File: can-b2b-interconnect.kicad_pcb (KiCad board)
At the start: 2 copper layers, 6.3 x 13.1 mm, 4 parts, among them U1 DF52-4S-0.8H(21), U2 DF52-4S-0.8H(21), U3 DF52-4S-0.8H(21)

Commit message: not routed yet, sch
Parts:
- removed U2, U3: DF52-4S-0.8H(21), can-b2b-interconnect:DF52-4S-0.8H(21)
- added J1: USB4110GFA, can-b2b-interconnect:GCT_USB4105-GF-A, F.Cu at (102.5, 63.5)
- added J2: USB4110GFA, can-b2b-interconnect:GCT_USB4105-GF-A, F.Cu at (102.5, 73.5)

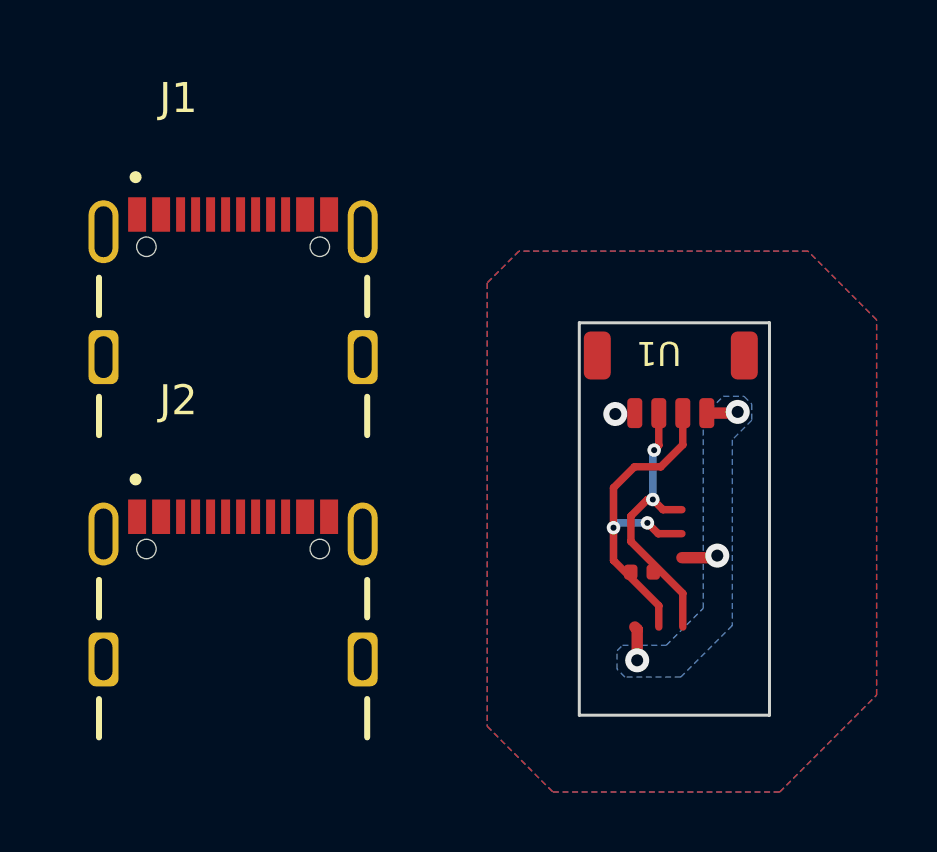
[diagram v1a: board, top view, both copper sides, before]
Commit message: df52 to two usbcs, with optional termination resistor
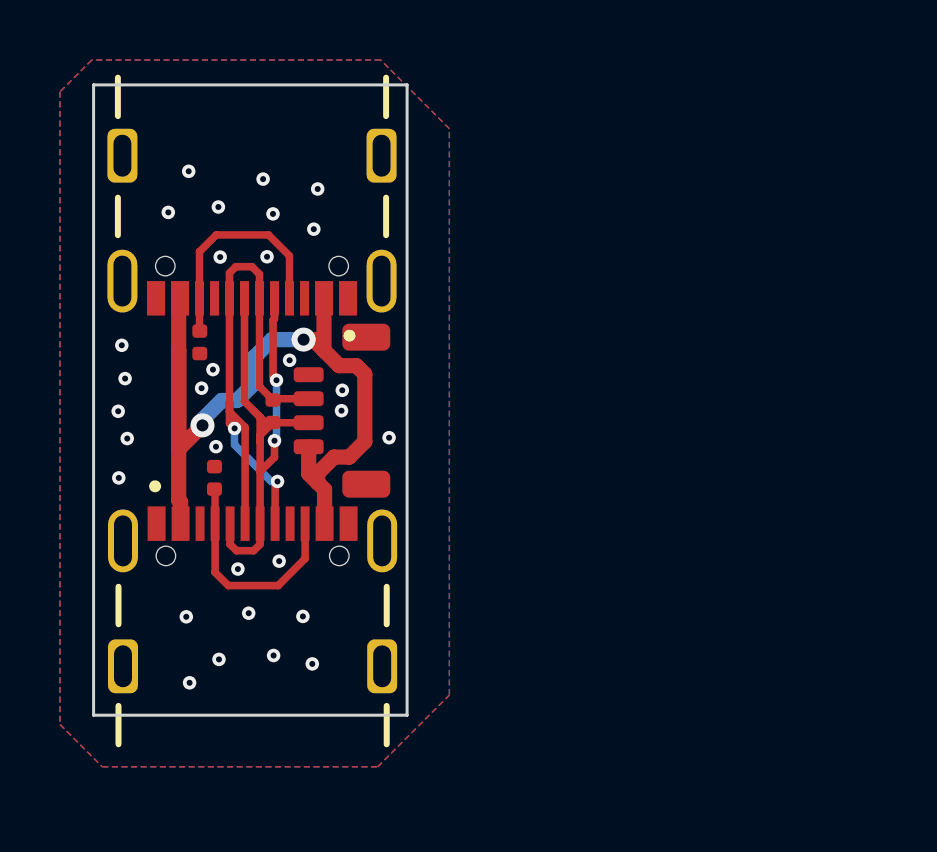
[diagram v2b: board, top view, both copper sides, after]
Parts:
- added R2: 5.1k, can-b2b-interconnect:R_0402_1005Metric, F.Cu at (101.3, 63.0)
- added R3: 5.1k, can-b2b-interconnect:R_0402_1005Metric, F.Cu at (101.8, 67.5)
- moved R1 13.4 mm to (103.8, 65.3), turned to 90 degrees
- moved U1 12.1 mm to (105.0, 65.2), turned to 90 degrees
- moved J1 6.74 mm to (103.1, 56.8), turned to 180 degrees
- moved J2 0.69 mm to (103.1, 73.8)
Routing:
- net /VBAT: track 3.40 -> 28.8 mm, vias 3 -> 2
- net /CANH: track 9.45 -> 20.2 mm
- net Net-(J1-CC1): track 0.00 -> 7.59 mm
- net Net-(J2-CC1): track 0.00 -> 7.50 mm
- net /CANL: track 11.7 -> 19.2 mm
- net GND: vias 1 -> 30
- removed copper zone on B.Cu, net /VBAT
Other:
- board size 6.3 x 13.1 mm -> 10.5 x 21 mm

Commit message: board designed
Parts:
- removed J1: USB4110GFA, can-b2b-interconnect:GCT_USB4105-GF-A
- removed R2: 5.1k, can-b2b-interconnect:R_0402_1005Metric
- moved U1 2.04 mm to (103.1, 66.0), turned to 180 degrees
- moved R1 2.03 mm to (103.1, 67.2), turned to 180 degrees
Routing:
- net /VBAT: track 28.8 -> 13.1 mm
- net /CANH: track 20.2 -> 6.85 mm
- net /CANL: track 19.2 -> 7.61 mm, vias 2 -> 0
- net Net-(J1-CC1): track 7.59 -> 0.00 mm
- net Net-(J2-CC1): track 7.50 -> 8.76 mm
- net GND: vias 30 -> 1
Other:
- board size 10.5 x 21 mm -> 10.3 x 11.8 mm
